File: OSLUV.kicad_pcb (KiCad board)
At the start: 4 copper layers, 110 x 85 mm, 198 parts, among them IC1 NCP12510ASN65T1G, IC2 SFH6156-3, IC3 INA210, IC4 AP63300WU-7, IC5 AP63300WU-7, IC6 STM32G071KBT6, IC7 TLV9001IDBVR, IC8 FAN3100TSX, J1 B08B-XASK-1-A_LF__SN_, J3 BM02B-SRSS-TB_LF__SN_, J4 BM02B-SRSS-TB_LF__SN_, J5 640445-2, J6 640445-2, J7 B5P-VH, Q1 STD3NK80ZT4, Q2 BAT847B, Q3 BSS138, Q4 BC807, Q5 BC807, T1 750343466, T4 NMOS_GDS-KS_SMD, U1 OPA2356AIDGKR, U2 AZ431LANTR, U3 LM2904, U4 Prog

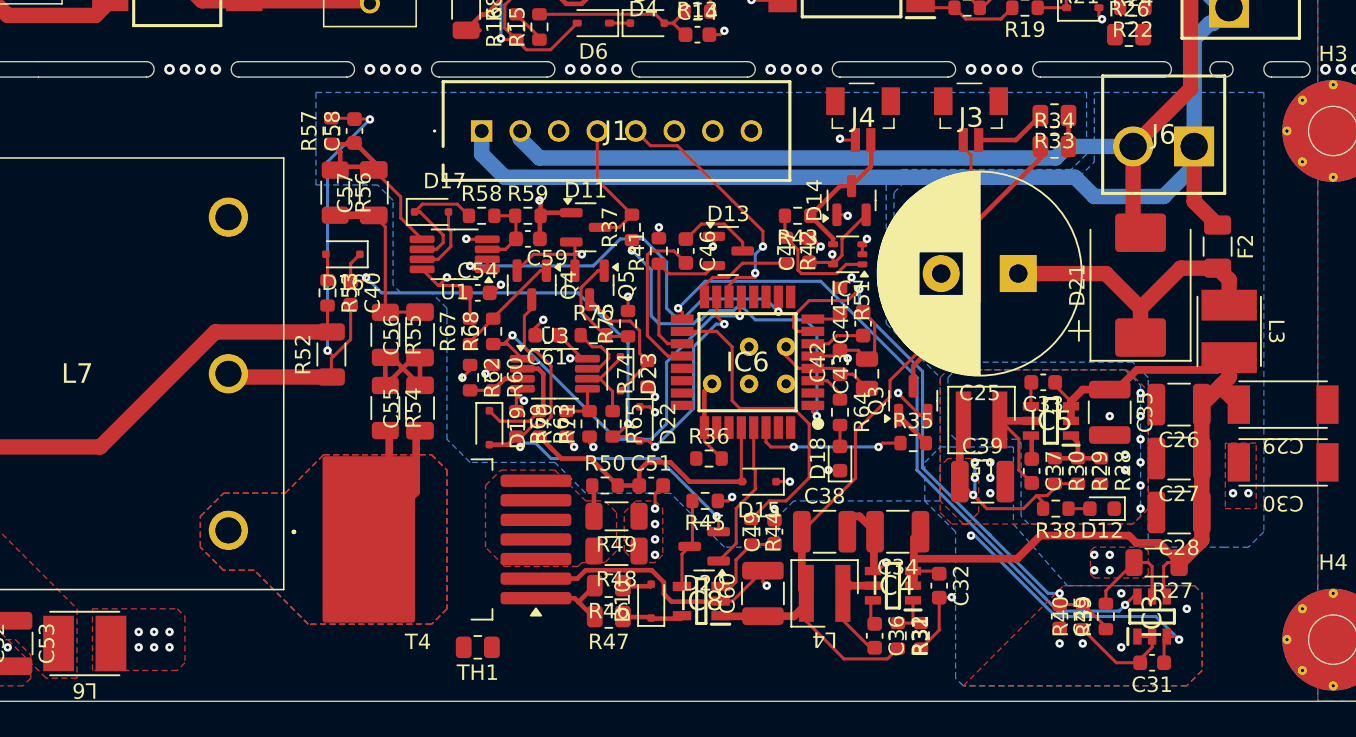
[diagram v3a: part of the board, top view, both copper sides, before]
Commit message: initial version of excimer driver PCB
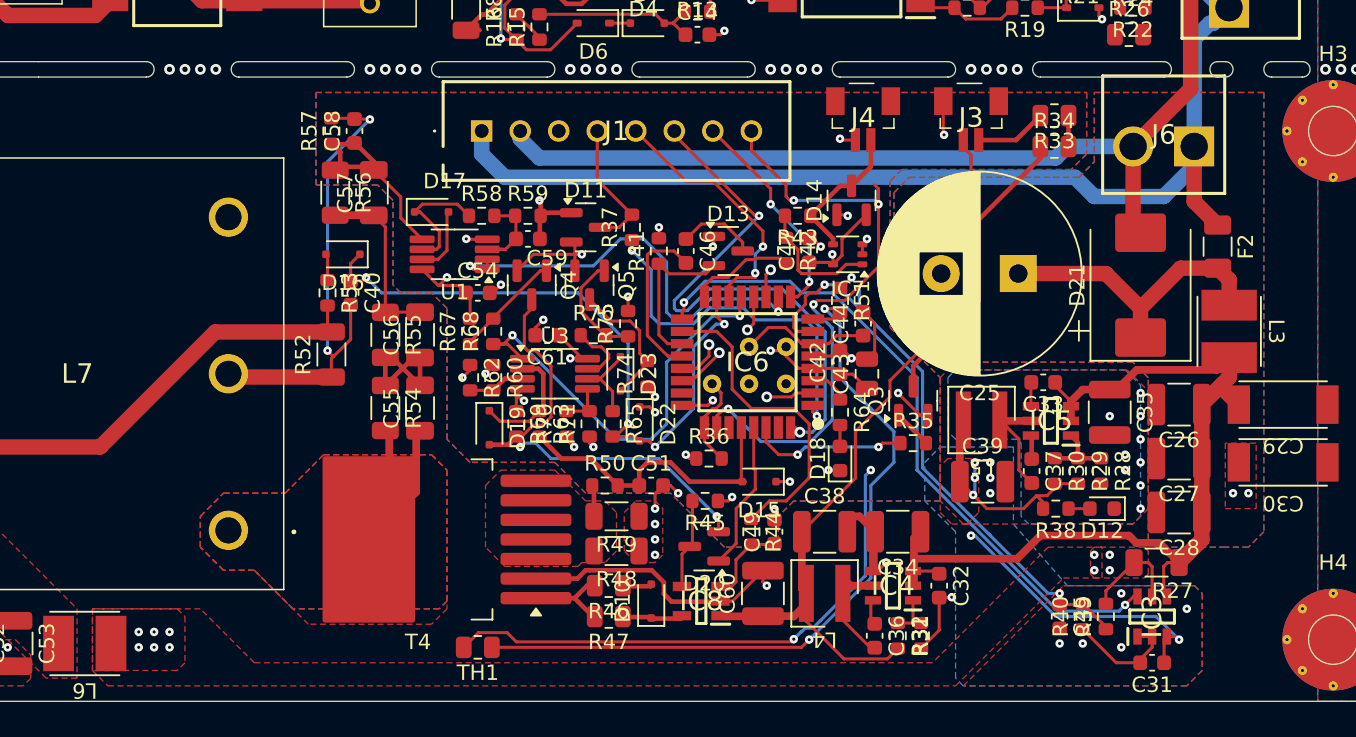
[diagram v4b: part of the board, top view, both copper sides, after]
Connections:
- C44 pad 1: /excimerDriver/RESET -> unconnected-(C44-Pad1)
- IC6 pad 11: /excimerDriver/Ilevel_DAC -> unconnected-(IC6-PA4-Pad11)
- IC6 pad 22: /excimerDriver/PeakCurrent -> unconnected-(IC6-PA11_[PA9]-Pad22)
- IC6 pad 24: unconnected-(IC6-PA13-Pad24) -> /excimerDriver/SWDIO
- IC6 pad 32: unconnected-(IC6-PB8-Pad32) -> /excimerDriver/PWM
- J1 pad 7: /excimerDriver/UART_TX -> /excimerDriver/CMD_TX
- J1 pad 8: /excimerDriver/UART_RX -> /excimerDriver/CMD_RX
- R36 pad 2: unconnected-(R36-Pad2) -> /excimerDriver/SWCLK
- R54 pad 1: Net-(R54-Pad1) -> /excimerDriver/lampDriver/HV_Drain_div
- R55 pad 2: Net-(R54-Pad1) -> /excimerDriver/lampDriver/HV_Drain_div
- U4 pad 1: unconnected-(U4-MCLR-Pad1) -> /excimerDriver/RESET
- U4 pad 3: unconnected-(U4-VSS-Pad3) -> GND
- U4 pad 4: unconnected-(U4-DAT-Pad4) -> /excimerDriver/SWDIO
- U4 pad 5: unconnected-(U4-CLK-Pad5) -> /excimerDriver/SWCLK
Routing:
- net /excimerDriver/temp_MOSFET: track 1.92 -> 49.5 mm, vias 0 -> 2
- net /excimerDriver/CMD_RX: track 0.00 -> 40.0 mm, vias 0 -> 4
- net GND: track 217.3 -> 256.3 mm, vias 62 -> 67
- net /excimerDriver/PWM: track 0.00 -> 36.2 mm, vias 0 -> 2
- net /excimerDriver/CMD_TX: track 0.00 -> 14.1 mm, vias 0 -> 2
- net /excimerDriver/lampDriver/HV_Drain_div: track 0.00 -> 9.63 mm
- net (no net): track 9.63 -> 0.00 mm
- net /excimerDriver/RESET: track 3.48 -> 8.57 mm
- net /excimerDriver/SWDIO: track 0.00 -> 4.96 mm, vias 0 -> 1
- net unconnected-(IC6-PA11_[PA9]-Pad22): track 0.00 -> 3.19 mm, vias 0 -> 1
- net unconnected-(IC6-PC14-OSC32_IN-Pad2): track 0.00 -> 3.10 mm, vias 0 -> 1
- net unconnected-(IC6-PA10-Pad21): track 0.00 -> 2.82 mm, vias 0 -> 1
- net /excimerDriver/DAC2: track 0.00 -> 2.31 mm, vias 0 -> 1
- net unconnected-(IC6-PA4-Pad11): track 0.00 -> 1.89 mm, vias 0 -> 1
- net /excimerDriver/SWCLK: track 5.52 -> 7.13 mm
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
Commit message: error correction
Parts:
- moved L3 0.25 mm to (149.0, 111.0)
- moved R18 0.15 mm to (147.0, 63.4)
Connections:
- C44 pad 1: unconnected-(C44-Pad1) -> /excimerDriver/RESET
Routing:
- net /excimerDriver/VDC_filter: track 58.5 -> 46.0 mm
- net /offlineConverter/PDC_CM: track 36.2 -> 38.8 mm
- net /offlineConverter/N: track 11.3 -> 10.5 mm
- net /excimerDriver/Status: track 16.8 -> 16.2 mm
- net GND: track 256.3 -> 256.9 mm
- net (no net): vias 24 -> 0
- added copper zone on F.Cu, net /excimerDriver/VDC_filter
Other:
- outline, holes or cut-outs redrawn

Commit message: error correction
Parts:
- removed D23: BAT54J, Diode_SMD:D_SOD-323F
- removed Q5: BC807, Package_TO_SOT_SMD:SOT-23
- removed R74: 100k 0603, Resistor_SMD:R_0603_1608Metric
- removed R75, R76: 10k 0603, Resistor_SMD:R_0603_1608Metric
- added R61: 10k 0603, Resistor_SMD:R_0603_1608Metric, F.Cu at (106.0, 107.5)
- added R66: 2k2 0603, Resistor_SMD:R_0603_1608Metric, F.Cu at (104.2, 107.5)
- added REF**: Loch_0,3mm, Hansmann:Loch_0,3mm, F.Cu at (96.5, 94.0)
- added REF**: Loch_0,3mm, Hansmann:Loch_0,3mm, F.Cu at (108.5, 94.0)
- added REF**: Loch_0,3mm, Hansmann:Loch_0,3mm, F.Cu at (80.5, 94.0)
- added REF**: Loch_0,3mm, Hansmann:Loch_0,3mm, F.Cu at (109.5, 94.0)
- added REF**: Loch_0,3mm, Hansmann:Loch_0,3mm, F.Cu at (122.5, 94.0)
- added REF**: Loch_0,3mm, Hansmann:Loch_0,3mm, F.Cu at (68.5, 94.0)
- added REF**: Loch_0,3mm, Hansmann:Loch_0,3mm, F.Cu at (134.5, 94.0)
- added REF**: Loch_0,3mm, Hansmann:Loch_0,3mm, F.Cu at (81.5, 94.0)
- added REF**: Loch_0,3mm, Hansmann:Loch_0,3mm, F.Cu at (119.5, 94.0)
- added REF**: Loch_0,3mm, Hansmann:Loch_0,3mm, F.Cu at (120.5, 94.0)
- added REF**: Loch_0,3mm, Hansmann:Loch_0,3mm, F.Cu at (70.5, 94.0)
- added REF**: Loch_0,3mm, Hansmann:Loch_0,3mm, F.Cu at (107.5, 94.0)
- added REF**: Loch_0,3mm, Hansmann:Loch_0,3mm, F.Cu at (95.5, 94.0)
- added REF**: Loch_0,3mm, Hansmann:Loch_0,3mm, F.Cu at (94.5, 94.0)
- added REF**: Loch_0,3mm, Hansmann:Loch_0,3mm, F.Cu at (82.5, 94.0)
- added REF**: Loch_0,3mm, Hansmann:Loch_0,3mm, F.Cu at (67.5, 94.0)
- added REF**: Loch_0,3mm, Hansmann:Loch_0,3mm, F.Cu at (106.5, 94.0)
- added REF**: Loch_0,3mm, Hansmann:Loch_0,3mm, F.Cu at (132.5, 94.0)
- added REF**: Loch_0,3mm, Hansmann:Loch_0,3mm, F.Cu at (121.5, 94.0)
- added REF**: Loch_0,3mm, Hansmann:Loch_0,3mm, F.Cu at (83.5, 94.0)
- added REF**: Loch_0,3mm, Hansmann:Loch_0,3mm, F.Cu at (69.5, 94.0)
- added REF**: Loch_0,3mm, Hansmann:Loch_0,3mm, F.Cu at (133.5, 94.0)
- added REF**: Loch_0,3mm, Hansmann:Loch_0,3mm, F.Cu at (93.5, 94.0)
- added REF**: Loch_0,3mm, Hansmann:Loch_0,3mm, F.Cu at (135.5, 94.0)
- U1: footprint Package_SO:VSSOP-8_3x3mm_P0.65mm -> Package_SO:VSSOP-8_3.0x3.0mm_P0.65mm
- U3: value LM2904 -> LM2902; footprint Package_SO:VSSOP-8_3x3mm_P0.65mm -> Package_SO:TSSOP-14_4.4x5mm_P0.65mm
- moved R62 12.3 mm to (112.0, 116.5), turned to 90 degrees
- moved D22 10.7 mm to (101.0, 113.2), turned to 90 degrees
- moved R71 10.3 mm to (100.0, 110.2), turned to 0 degrees
- moved R60 9.34 mm to (110.5, 116.5), turned to 90 degrees
- moved Q4 9.20 mm to (101.5, 116.8)
- moved R69 8.00 mm to (110.8, 119.0), turned to 180 degrees
- moved R70 7.60 mm to (102.8, 110.2), turned to -90 degrees
- moved D19 7.54 mm to (108.8, 116.5)
- moved R65 7.50 mm to (102.8, 113.2)
- moved R67 6.80 mm to (104.0, 116.5), turned to -90 degrees
- moved R68 6.80 mm to (105.5, 116.5), turned to -90 degrees
- moved C61 4.65 mm to (108.8, 108.5)
- moved U3 2.66 mm to (107.5, 112.0), turned to 180 degrees
- moved R63 2.55 mm to (107.0, 116.5)
- moved C54 0.75 mm to (99.8, 108.5)
- renumbered C1 to C101, C2 to C102, C3 to C103, C4 to C104, C5 to C105, C6 to C106, C24 to C107, C17 to C108, C16 to C109, C25 to C110, L1 to L101, L2 to L102, L7 to L103, T1 to L104
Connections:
- D2 pad 2: /offlineConverter/Drain -> Net-(D2-A)
- L104 pad 3: /offlineConverter/Drain -> unconnected-(L104-N1_1-Pad3)
- Q1 pad 2: /offlineConverter/Drain -> Net-(D2-A)
- R65 pad 1: Net-(D23-K) -> Net-(U3D--)
- R70 pad 2: Net-(U3B-+) -> Net-(U3D-+)
- R71 pad 2: Net-(U3B-+) -> Net-(U3D-+)
- U1 pad 6: Net-(D17-K) -> unconnected-(U1B---Pad6)
- U3 pad 4: GND -> +3V3
- U3 pad 5: Net-(U3B-+) -> GND
- U3 pad 6: Net-(D23-K) -> unconnected-(U3B---Pad6)
- U3 pad 7: /excimerDriver/OCP_Sec -> unconnected-(U3-Pad7)
- U3 pad 8: +3V3 -> /excimerDriver/OCP
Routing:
- net Net-(D2-A): track 0.00 -> 16.6 mm, vias 0 -> 36
- net /offlineConverter/Drain: track 16.6 -> 0.00 mm, vias 42 -> 0
- net /excimerDriver/VDC: track 122.4 -> 139.0 mm
- net Net-(D19-A): track 30.2 -> 21.3 mm
- net Net-(D23-A): track 8.92 -> 0.00 mm
- net Net-(Q5-B): track 7.22 -> 0.00 mm
- net /excimerDriver/Usense_Lamp: track 28.4 -> 34.4 mm
- net Net-(U3C-+): track 0.00 -> 5.77 mm
- net +3V3: track 74.7 -> 80.3 mm, vias 16 -> 14
- net Net-(C108-Pad1): track 0.00 -> 5.50 mm
- net Net-(D23-K): track 5.23 -> 0.00 mm
- net Net-(U3D-+): track 0.00 -> 5.06 mm
- net /excimerDriver/OCP_Sec: track 4.09 -> 0.00 mm
- net Net-(Q4-B): track 7.04 -> 3.88 mm
- net Net-(U3B-+): track 3.01 -> 0.00 mm
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- added copper zone on F.Cu, net Net-(D2-A)
- added copper zone on B.Cu, net unconnected-(L104-N1_1-Pad3)
- added copper zone on In1.Cu, net unconnected-(L104-N1_1-Pad3)
- added copper zone on In2.Cu, net unconnected-(L104-N1_1-Pad3)
- removed copper zone on B.Cu, net /offlineConverter/Drain
- removed copper zone on F.Cu, net /offlineConverter/Drain
- removed copper zone on In1.Cu, net /offlineConverter/Drain
- removed copper zone on In2.Cu, net /offlineConverter/Drain
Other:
- outline, holes or cut-outs redrawn

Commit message: alpha prototype
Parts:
- C9: value 100pF NP0 0603 -> 100pF NP0 1206
- R26: value 51 0805 -> 51R 0805
- R51: value 10k 0603 -> 18k 0603
- T4: value NMOS_GDS-KS_SMD -> IMBG120R181M2HXTMA1
- TH1: value NTC xxx -> PTC 680R 80°C
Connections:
- D2 pad 2: Net-(D2-A) -> /offlineConverter/Drain
- IC6 pad 7: /excimerDriver/24V_Sense -> unconnected-(IC6-PA0-Pad7)
- L104 pad 3: unconnected-(L104-N1_1-Pad3) -> /offlineConverter/Drain
- Q1 pad 2: Net-(D2-A) -> /offlineConverter/Drain
- U1 pad 6: unconnected-(U1B---Pad6) -> Net-(D17-K)
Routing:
- net Net-(D2-A): track 16.6 -> 0.00 mm, vias 36 -> 0
- net /offlineConverter/Drain: track 0.00 -> 16.6 mm, vias 0 -> 42
- net GND: track 259.5 -> 261.8 mm, vias 64 -> 67
- net unconnected-(L104-N1_1-Pad3): vias 6 -> 0
- added copper zone on B.Cu, net /offlineConverter/Drain
- added copper zone on F.Cu, net /offlineConverter/Drain
- added copper zone on In1.Cu, net /offlineConverter/Drain
- added copper zone on In2.Cu, net /offlineConverter/Drain
- removed copper zone on F.Cu, net Net-(D2-A)
- removed copper zone on B.Cu, net unconnected-(L104-N1_1-Pad3)
- removed copper zone on In1.Cu, net unconnected-(L104-N1_1-Pad3)
- removed copper zone on In2.Cu, net unconnected-(L104-N1_1-Pad3)

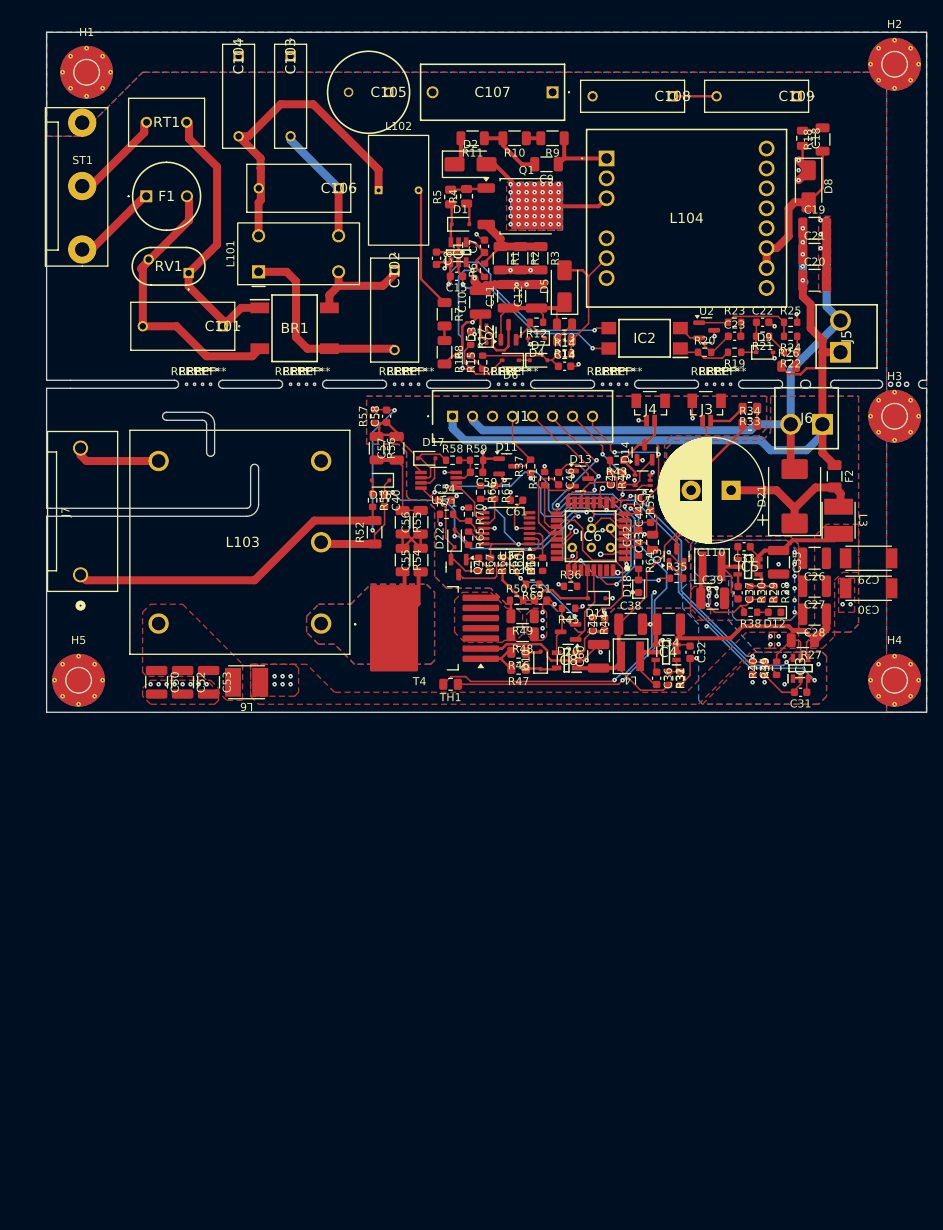
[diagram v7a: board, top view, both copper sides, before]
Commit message: error correction first prototype
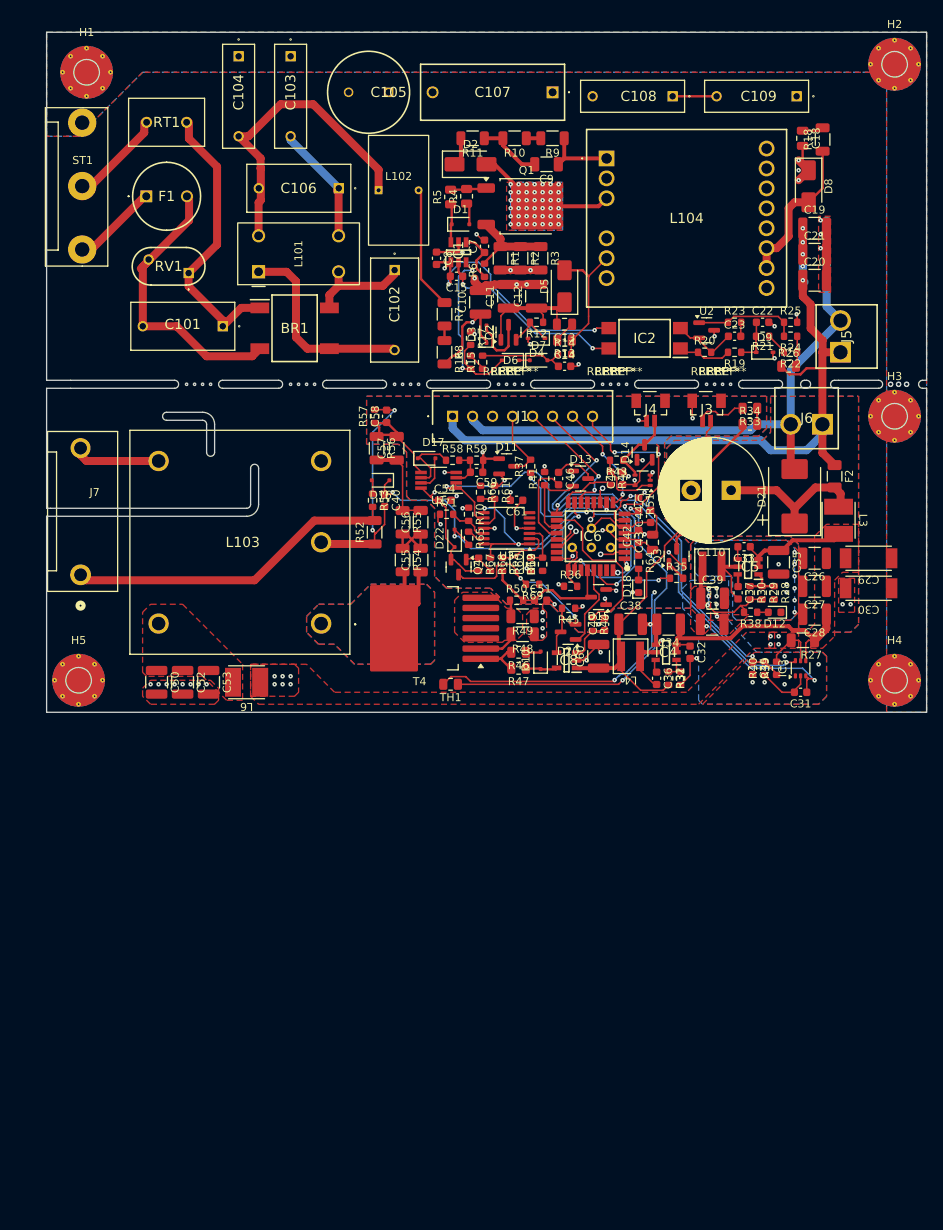
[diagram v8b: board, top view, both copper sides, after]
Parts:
- added C1: 10u X7R 1210, Capacitor_SMD:C_1210_3225Metric, F.Cu at (133.2, 124.0)
- D15: value BAT54J -> BAS40-04; footprint Diode_SMD:D_SOD-323F -> Package_TO_SOT_SMD:SOT-23
- IC3: footprint Hansmann:SOT95P280X90-6N -> Package_TO_SOT_SMD:SOT-363_SC-70-6
- R45: value 100k 0603 -> 10k 0603
- R47: value 33R 0805 -> 150R 0805
- moved D15 0.29 mm to (119.0, 120.6)
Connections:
- D15 pad 1: +3V3 -> GND
- D15 pad 2: /excimerDriver/Isense_MOS -> +3V3
- IC3 pad 3: +3V3 -> unconnected-(IC3-VCC-Pad3)
- IC6 pad 11: unconnected-(IC6-PA4-Pad11) -> /excimerDriver/Ilevel_DAC
- IC6 pad 7: unconnected-(IC6-PA0-Pad7) -> /excimerDriver/24V_Sense
- J3 pad 1: Net-(J3-Pad1) -> +15V
- J3 pad 2: +15V -> Net-(J3-Pad2)
- R33 pad 2: Net-(J3-Pad1) -> Net-(J3-Pad2)
- T4 pad 3: GND -> unconnected-(T4-KS-Pad3)
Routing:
- net GND: track 261.8 -> 247.3 mm, vias 67 -> 69
- net Net-(J3-Pad2): track 0.00 -> 6.81 mm
- net /excimerDriver/lampDriver/Source: track 1.89 -> 6.81 mm
- net Net-(J3-Pad1): track 4.66 -> 0.00 mm
- net unconnected-(IC6-PA4-Pad11): track 1.89 -> 0.00 mm, vias 1 -> 0
- net /excimerDriver/Ilevel_DAC: track 0.00 -> 1.89 mm, vias 0 -> 1
- net +3V3: track 80.3 -> 81.2 mm
- net /excimerDriver/DRV_Mask: track 9.69 -> 10.4 mm
